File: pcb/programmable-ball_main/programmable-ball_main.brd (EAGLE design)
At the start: 29 x 29 mm, 19 parts, among them J1 12402012E212A, P1 S2B-ZR-SM4A-TF, Q1 DMG2305UX-13, SW1 CAS-120CAS-120B1, U1 MDBT50Q-1MV2, U2 AP2112K-3.3TRG1, Y1 FC-135_32.7680KA-A0

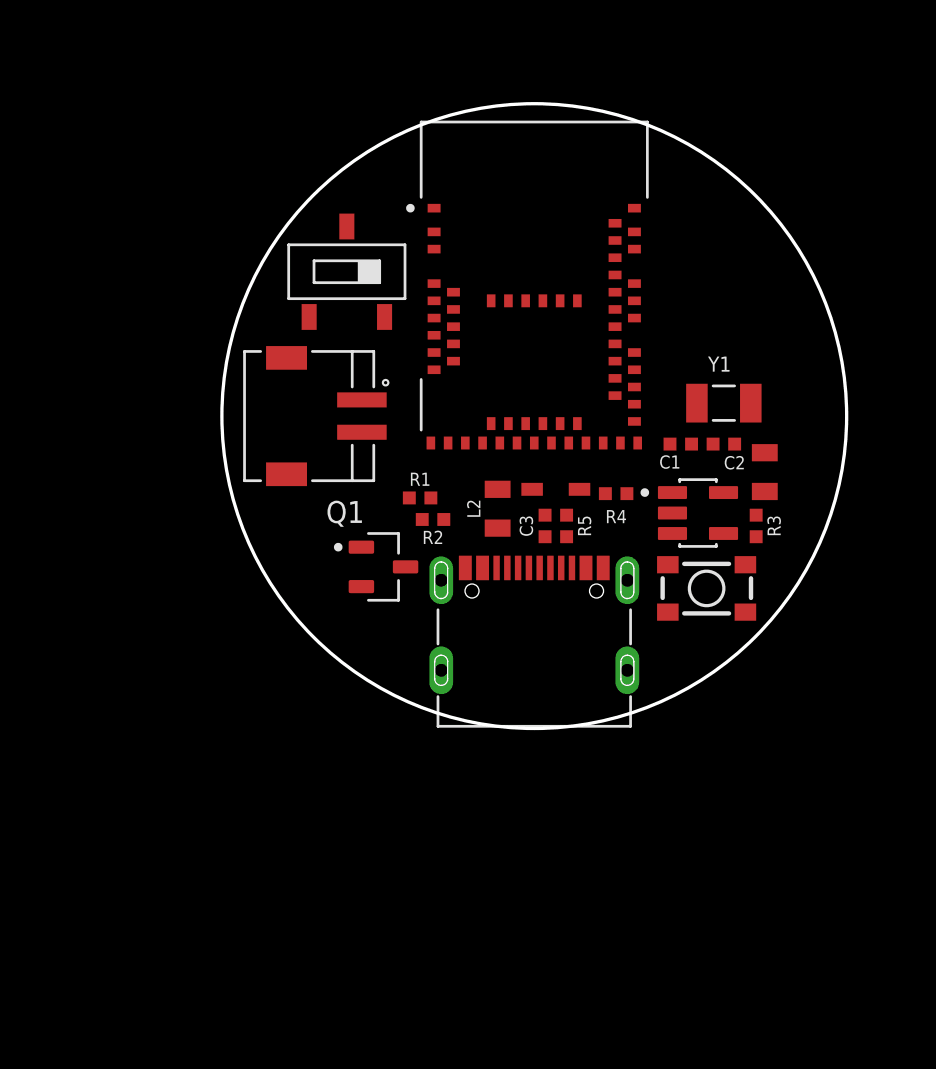
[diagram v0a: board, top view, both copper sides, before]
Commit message: 主電源スイッチとリポ充放電素子を追加 #4
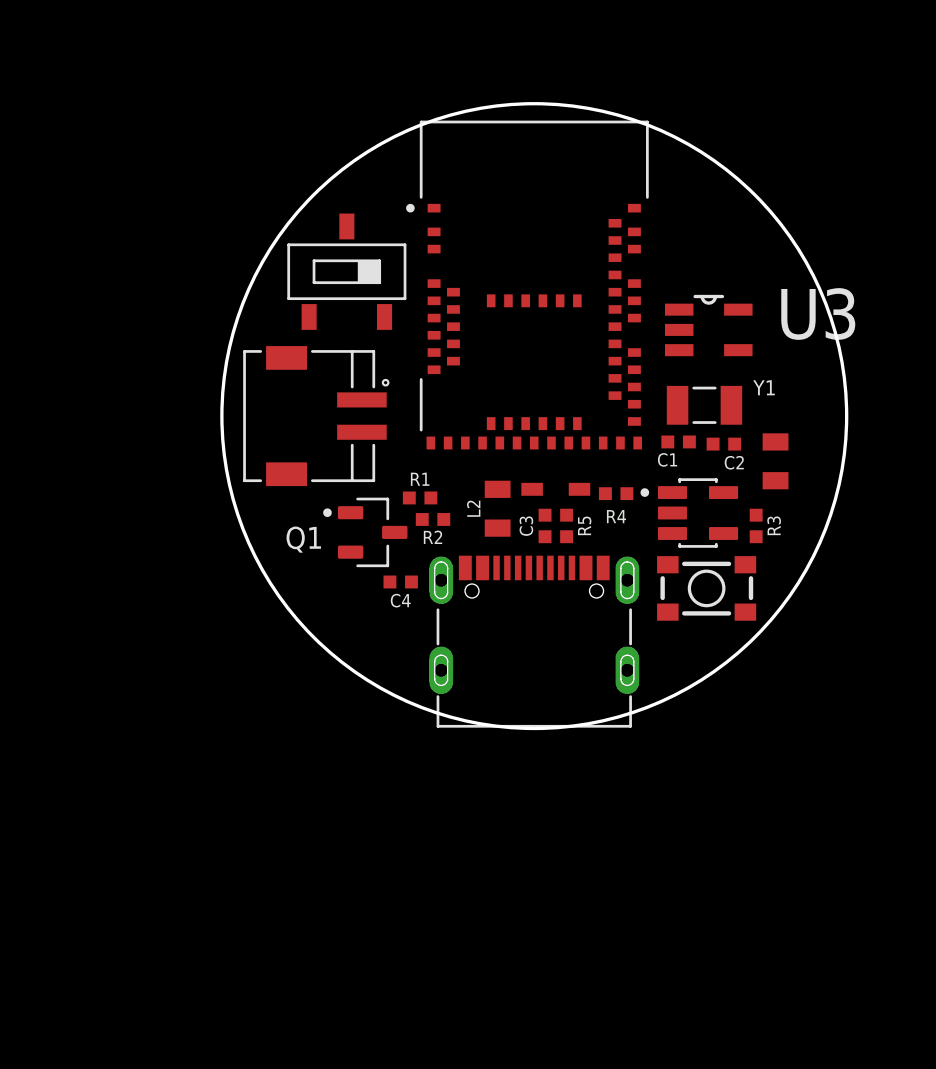
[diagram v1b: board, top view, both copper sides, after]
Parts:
- added C4: 10uF, SparkFun-Capacitors:0402-TIGHT
- added U3: MCP73832T-2ACI/OT, MCP73832T-2ACI_OT:SOT95P270X145-5N
- moved Q1 1.68 mm to (7.50, 9.60)
- moved Y1 0.91 mm to (22.9, 15.5)
- moved L1 0.71 mm to (26.2, 12.9)
- moved C1 0.14 mm to (21.7, 13.8)
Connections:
- removed net I2C_SCL: U1.49
- removed net I2C_SDA: U1.19
- new net EN: R4.1, SW1.2, U2.3
- new net N$8: U3.1
- net GND: now also C4.1, SW1.1, U3.2
- net N$7: now also U3.5; no longer R4.1, U2.3
- net VBAT: now also C4.2, U3.3
- net VBUS: now also U3.4

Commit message: リポ充放電機能を搭載 #4
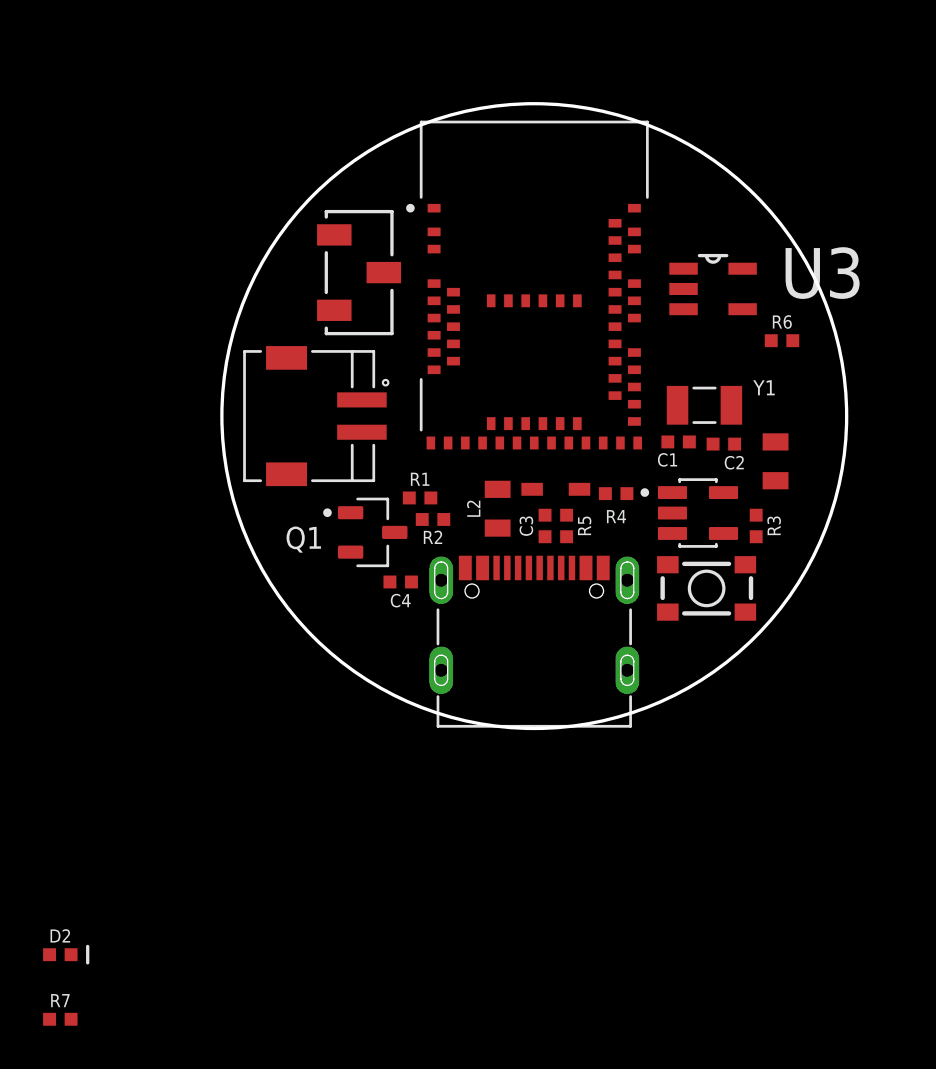
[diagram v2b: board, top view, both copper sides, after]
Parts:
- removed SW1: CAS-120CAS-120B1, Switch:CAS-120B1
- added D2: RED, SparkFun-LED:LED-0402
- added R6: 4.7k, SparkFun-Resistors:0402-TIGHT
- added R7: 1k, SparkFun-Resistors:0402-TIGHT
- added S2: CASA-120TA-PB, CAS_120TA:CAS-120A
- moved U3 1.91 mm to (23.3, 20.9)
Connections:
- new net N$9: D2.A, R7.2
- net EN: now also S2.2; no longer SW1.2
- net GND: now also R6.1, S2.3; no longer SW1.1
- net N$7: now also R6.2
- net N$8: now also D2.C
- net VBUS: now also R7.1
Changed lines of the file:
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@@
 <attribute name="PROD_ID" value="CAP-14848" x="15.5" y="9.9" size="1.778" layer="27" rot="R90" display="off"/>
 </element>
-<element name="SW1" library="Switch" package="CAS-120B1" value="CAS-120CAS-120B1" x="6.3" y="21.7" smashed="yes"/>
-<element name="U3" library="MCP73832T-2ACI_OT" package="SOT95P270X145-5N" value="MCP73832T-2ACI/OT" x="23.1" y="19" smashed="yes">
-<attribute name="NAME" x="26.216859375" y="18.58273125" size="2.315940625" layer="25"/>
+<element name="U3" library="MCP73832T-2ACI_OT" package="SOT95P270X145-5N" value="MCP73832T-2ACI/OT" x="23.3" y="20.9" smashed="yes">
+<attribute name="NAME" x="26.416859375" y="20.48273125" size="2.315940625" layer="25"/>
 </element>
 <element name="C4" library="SparkFun-Capacitors" package="0402-TIGHT" value="10uF" x="8.8" y="7.3" smashed="yes" rot="R180">
 <attribute name="NAME" x="8.8" y="6.738" size="0.6096" layer="25" font="vector" ratio="20" rot="R180" align="bottom-center"/>
 <attribute name="PROD_ID" value="CAP-14848" x="8.8" y="7.3" size="1.778" layer="27" rot="R180" display="off"/>
+</element>
+<element name="S2" library="CAS_120TA" package="CAS-120A" value="CASA-120TA-PB" x="5.6" y="24.2" smashed="yes" rot="R270"/>
+<element name="R6" library="SparkFun-Resistors" package="0402-TIGHT" value="4.7k" x="26.5" y="18.5" smashed="yes">
+<attribute name="NAME" x="26.5" y="19.062" size="0.6096" layer="25" font="vector" ratio="20" align="bottom-center"/>
+<attribute name="PROD_ID" value="RES-15343" x="26.5" y="18.5" size="1.778" layer="27" display="off"/>
+</element>
+<element name="D2" library="SparkFun-LED" package="LED-0402" value="RED" x="-7" y="-10" smashed="yes">
+<attribute name="NAME" x="-7" y="-9.438" size="0.6096" layer="25" font="vector" ratio="20" align="bottom-center"/>
+<attribute name="PROD_ID" value="DIO-16757" x="-7" y="-10" size="1.778" layer="27" display="off"/>
+<attribute name="VALUE" x="-7" y="-10.562" size="0.6096" layer="27" font="vector" ratio="20" align="top-center"/>
+</element>
+<element name="R7" library="SparkFun-Resistors" package="0402-TIGHT" value="1k" x="-7" y="-13" smashed="yes">
+<attribute name="NAME" x="-7" y="-12.438" size="0.6096" layer="25" font="vector" ratio="20" align="bottom-center"/>
+<attribute name="PROD_ID" value="RES-14342" x="-7" y="-13" size="1.778" layer="27" display="off"/>
+<attribute name="VALUE" x="-7" y="-13.562" size="0.6096" layer="27" font="vector" ratio="20" align="top-center"/>
 </element>
 </elements>
@@
 <contactref element="R5" pad="1"/>
 <contactref element="C3" pad="1"/>
-<contactref element="SW1" pad="1"/>
 <contactref element="U3" pad="2"/>
 <contactref element="C4" pad="1"/>
-<wire x1="21.7284" y1="19" x2="19.65" y2="24.65" width="0" layer="19" extent="1-1"/>
-<wire x1="22.2" y1="13.8" x2="21.7284" y2="19" width="0" layer="19" extent="1-1"/>
+<contactref element="S2" pad="3"/>
+<contactref element="R6" pad="1"/>
+<wire x1="21.9284" y1="20.9" x2="19.65" y2="24.65" width="0" layer="19" extent="1-1"/>
+<wire x1="22.2" y1="13.8" x2="21.9284" y2="20.9" width="0" layer="19" extent="1-1"/>
 <wire x1="23.3" y1="13.7" x2="22.2" y2="13.8" width="0" layer="19" extent="1-1"/>
 <wire x1="19.8" y1="13.75" x2="22.2" y2="13.8" width="0" layer="19" extent="1-1"/>
@@
 <wire x1="13.3" y1="9.8" x2="15.5" y2="9.4" width="0" layer="19" extent="1-1"/>
 <wire x1="11.8" y1="7.95" x2="13.3" y2="9.8" width="0" layer="19" extent="1-1"/>
-<wire x1="9.8" y1="10.2" x2="11.8" y2="7.95" width="0" layer="19" extent="1-1"/>
+<wire x1="9.3" y1="7.3" x2="11.8" y2="7.95" width="0" layer="19" extent="1-1"/>
+<wire x1="9.8" y1="10.2" x2="9.3" y2="7.3" width="0" layer="19" extent="1-1"/>
 <wire x1="9.2" y1="11.2" x2="9.8" y2="10.2" width="0" layer="19" extent="1-1"/>
 <wire x1="10.2" y1="13.75" x2="9.2" y2="11.2" width="0" layer="19" extent="1-1"/>
 <wire x1="7" y1="14.25" x2="10.2" y2="13.75" width="0" layer="19" extent="1-1"/>
-<wire x1="9.3" y1="7.3" x2="11.8" y2="7.95" width="0" layer="19" extent="1-1"/>
-<wire x1="4.55" y1="19.6" x2="7" y2="14.25" width="0" layer="19" extent="1-1"/>
-<wire x1="10.35" y1="23.55" x2="4.55" y2="19.6" width="0" layer="19" extent="1-1"/>
+<wire x1="5.717" y1="19.91" x2="7" y2="14.25" width="0" layer="19" extent="1-1"/>
+<wire x1="10.35" y1="23.55" x2="5.717" y2="19.91" width="0" layer="19" extent="1-1"/>
 <wire x1="10.35" y1="24.65" x2="10.35" y2="23.55" width="0" layer="19" extent="1-1"/>
+<wire x1="26" y1="18.5" x2="9.3" y2="7.3" width="0" layer="19" extent="1-1"/>
 </signal>
 <signal name="VBUS">
@@
 <contactref element="D1" pad="2"/>
 <contactref element="U3" pad="4"/>
-<wire x1="19" y1="13.75" x2="24.4716" y2="18.0602" width="0" layer="19" extent="1-1"/>
+<contactref element="R7" pad="1"/>
+<wire x1="19" y1="13.75" x2="24.6716" y2="19.9602" width="0" layer="19" extent="1-1"/>
 <wire x1="17.1" y1="11.6" x2="19" y2="13.75" width="0" layer="19" extent="1-1"/>
 <wire x1="16.5" y1="10.4" x2="17.1" y2="11.6" width="0" layer="19" extent="1-1"/>
@@
 <wire x1="12.6" y1="7.95" x2="16.5" y2="10.4" width="0" layer="19" extent="1-1"/>
 <wire x1="6.475" y1="10.515" x2="12.6" y2="7.95" width="0" layer="19" extent="1-1"/>
+<wire x1="-7.5" y1="-13" x2="6.475" y2="10.515" width="0" layer="19" extent="1-1"/>
 </signal>
 <signal name="USBD+">
@@
 <contactref element="U3" pad="3"/>
 <contactref element="C4" pad="2"/>
-<wire x1="7" y1="15.75" x2="21.7284" y2="18.0602" width="0" layer="19" extent="1-1"/>
+<wire x1="7" y1="15.75" x2="21.9284" y2="19.9602" width="0" layer="19" extent="1-1"/>
 <wire x1="8.525" y1="9.6" x2="7" y2="15.75" width="0" layer="19" extent="1-1"/>
 <wire x1="8.3" y1="7.3" x2="8.525" y2="9.6" width="0" layer="19" extent="1-1"/>
@@
 <contactref element="U2" pad="3"/>
 <contactref element="R4" pad="1"/>
-<contactref element="SW1" pad="2"/>
+<contactref element="S2" pad="2"/>
 <wire x1="19.3" y1="11.4" x2="21.415" y2="9.55" width="0" layer="19" extent="1-1"/>
-<wire x1="6.3" y1="23.8" x2="19.3" y2="11.4" width="0" layer="19" extent="1-1"/>
+<wire x1="8.017" y1="21.66" x2="19.3" y2="11.4" width="0" layer="19" extent="1-1"/>
 </signal>
 <signal name="N$7">
 <contactref element="U3" pad="5"/>
+<contactref element="R6" pad="2"/>
+<wire x1="27" y1="18.5" x2="24.6716" y2="21.8398" width="0" layer="19" extent="1-1"/>
 </signal>
 <signal name="N$8">
 <contactref element="U3" pad="1"/>
+<contactref element="D2" pad="C"/>
+<wire x1="-6.5" y1="-10" x2="21.9284" y2="21.8398" width="0" layer="19" extent="1-1"/>
+</signal>
+<signal name="N$9">
+<contactref element="R7" pad="2"/>
+<contactref element="D2" pad="A"/>
+<wire x1="-7.5" y1="-10" x2="-6.5" y2="-13" width="0" layer="19" extent="1-1"/>
 </signal>
 </signals>

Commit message: パターンの位置調整
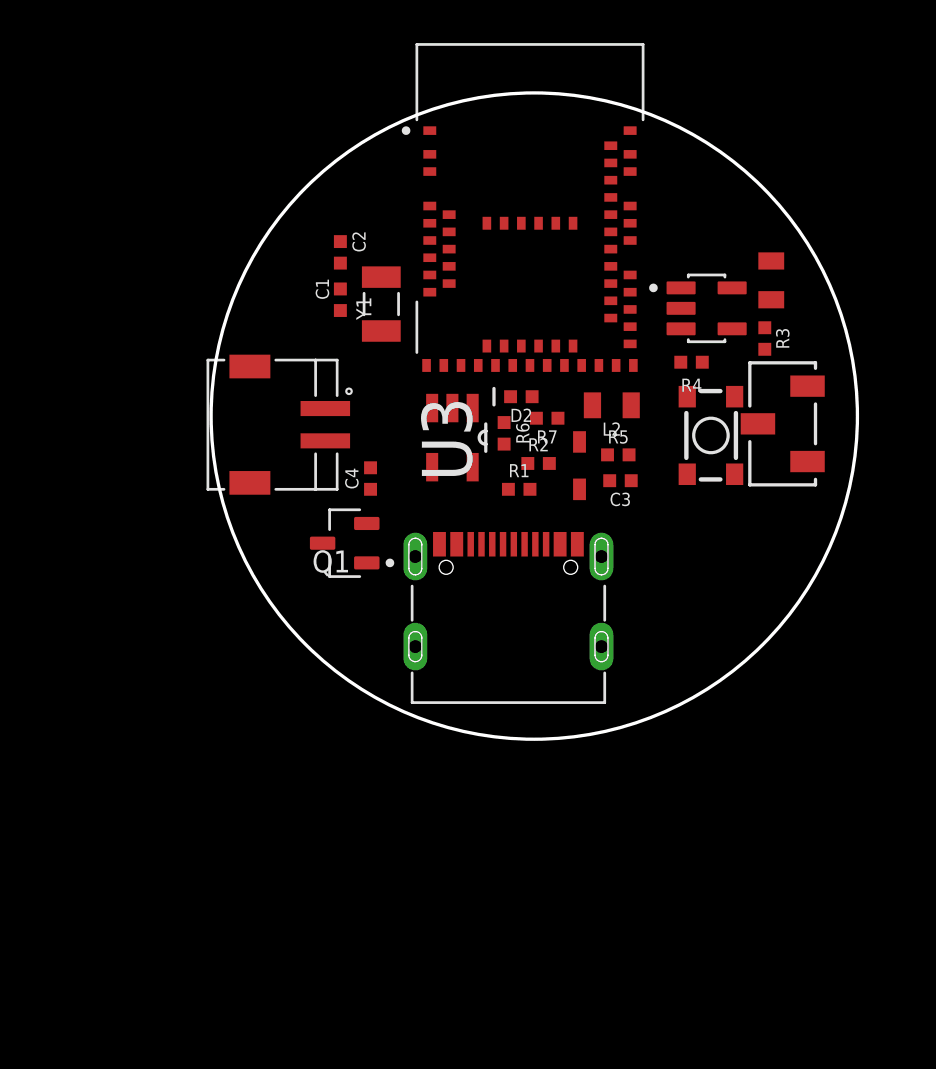
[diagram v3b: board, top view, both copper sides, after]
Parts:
- moved R7 35.9 mm to (15.6, 14.9), turned to 180 degrees
- moved D2 33.6 mm to (14.4, 15.9), turned to 180 degrees
- moved S2 25.3 mm to (27.8, 12.1), turned to 90 degrees
- moved C2 19.9 mm to (6.00, 22.6), turned to 270 degrees
- moved C1 17.0 mm to (6.00, 20.4), turned to 270 degrees
- moved Y1 15.7 mm to (7.90, 20.2), turned to 90 degrees
- moved U3 13.9 mm to (11.2, 14.0), turned to 270 degrees
- moved R6 13.6 mm to (13.6, 14.2), turned to 270 degrees
- moved U2 9.51 mm to (23.0, 20.0)
- moved R3 8.71 mm to (25.7, 18.6)
- moved L1 8.40 mm to (26.0, 21.3)
- moved L2 7.15 mm to (18.6, 15.5), turned to 0 degrees
- moved S1 7.10 mm to (23.2, 14.1), turned to 90 degrees
- moved R4 7.03 mm to (22.3, 17.5)
- moved R2 5.55 mm to (15.2, 12.8)
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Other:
- board size 29 x 29 mm -> 30 x 30 mm

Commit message: コネクタとコンデンサを追加 #4
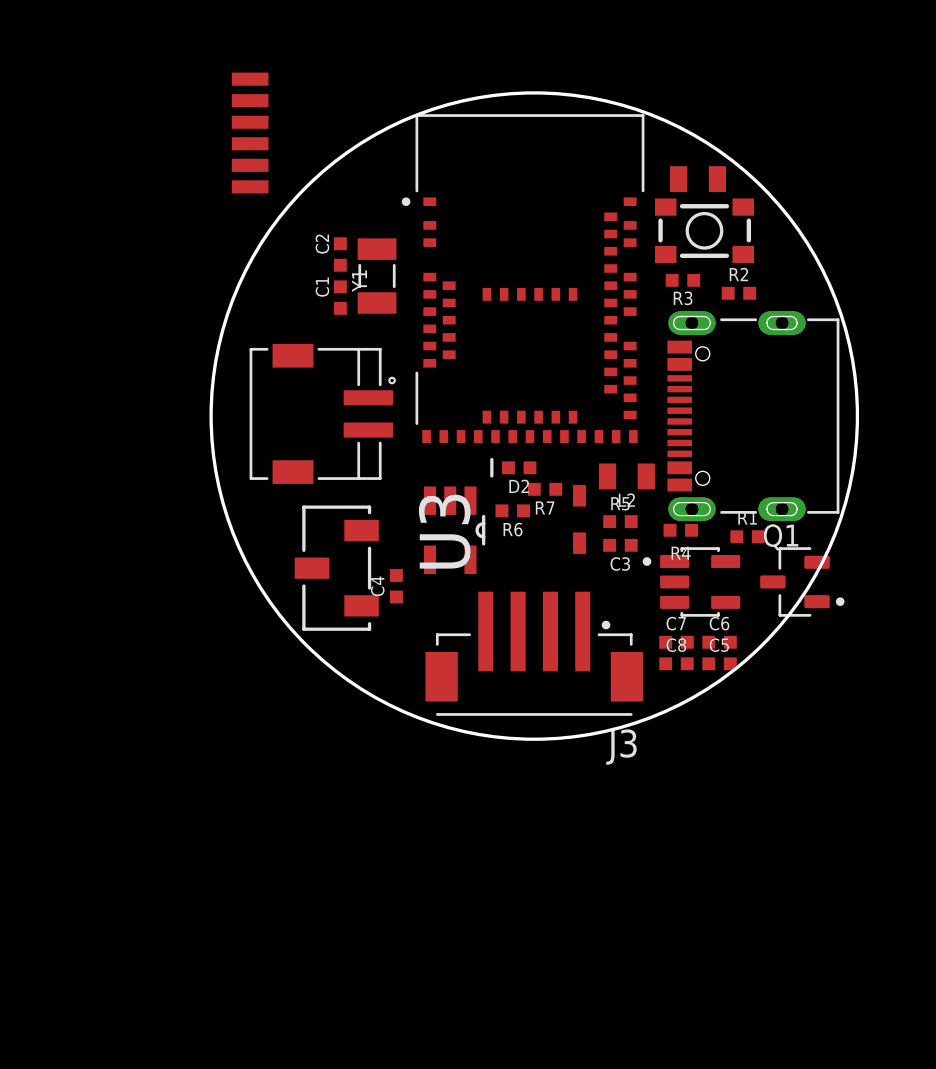
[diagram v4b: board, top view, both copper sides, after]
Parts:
- added C5, C6: 10uF, SparkFun-Capacitors:0402-TIGHT
- added C7, C8: 0.1uF, SparkFun-Capacitors:0402-TIGHT
- added DNP: 84981-6RE, JtagConnector:84981-6
- added J3: B4B-ZR-SM4-TFT(LF)(SN), B4B-ZR-SM4-TFT_LF__SN_:JST_B4B-ZR-SM4-TFT(LF)(SN)
- moved S2 21.8 mm to (7.10, 5.40)
- moved Q1 21.0 mm to (27.1, 7.30)
- moved J1 16.6 mm to (26.5, 15.0), turned to 90 degrees
- moved U2 12.7 mm to (22.7, 7.30)
- moved R2 12.2 mm to (24.5, 20.7)
- moved R1 10.8 mm to (24.9, 9.40)
- moved S1 9.50 mm to (22.9, 23.6), turned to 0 degrees
- moved R4 7.82 mm to (21.8, 9.70)
- moved L1 5.80 mm to (22.6, 26.0), turned to 0 degrees
- moved C4 5.14 mm to (8.60, 7.10)
- moved R3 4.66 mm to (21.9, 21.3), turned to 0 degrees
- moved U3 4.30 mm to (11.1, 9.70)
- moved R6 3.62 mm to (14.0, 10.6), turned to 180 degrees
- moved L2 3.37 mm to (19.3, 12.2)
- moved D2 3.30 mm to (14.3, 12.6)
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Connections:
- new net I2C_SCL: J3.2, U1.49
- new net I2C_SDA: J3.3, U1.19
- net 3.3V: now also C5.1, C7.1, C8.1, DNP.1, J3.1
- net GND: now also C5.2, C6.2, C7.2, C8.2, DNP.2, DNP.6, J3.4
- net RESET: now also DNP.5
- net SWDCLK: now also DNP.3
- net SWDIO: now also DNP.4
- net VBUS: now also C6.1
